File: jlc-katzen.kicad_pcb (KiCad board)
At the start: 2 copper layers, 50.8 x 50.8 mm, 46 parts, among them J1 USB_C_Receptacle_USB2.0_16P, J2 Conn_01x04, J3 Conn_01x04, J4 Conn_01x02, J5 Conn_ARM_SWD_TagConnect_TC2030, Q1 2N7002, Q2 2N7002, Q3 2N7002, U1 XC6206P332MR, U2 W25Q128JVSIQ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

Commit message: useless twiddles
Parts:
- moved J5 16.5 mm to (115.5, 42.1)
- moved J4 6.31 mm to (91.7, 62.1), turned to -90 degrees
- moved R2 4.12 mm to (87.0, 50.5)
- moved R1 4.03 mm to (87.0, 46.5)
- moved R10 3.04 mm to (94.5, 62.5)
- moved R8 2.55 mm to (94.5, 61.5)
- moved R6 2.50 mm to (91.0, 47.5)
- moved C17 2.23 mm to (87.5, 61.5)
- moved U2 2.06 mm to (90.5, 57.5)
- moved C16 1.80 mm to (100.0, 61.0)
- moved U4 1.80 mm to (103.5, 63.5)
- moved C8 1.58 mm to (106.0, 48.0)
- moved C9 1.58 mm to (106.0, 49.0)
- moved R3 1.58 mm to (106.0, 47.0)
- moved C13 1.12 mm to (97.0, 44.0)
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
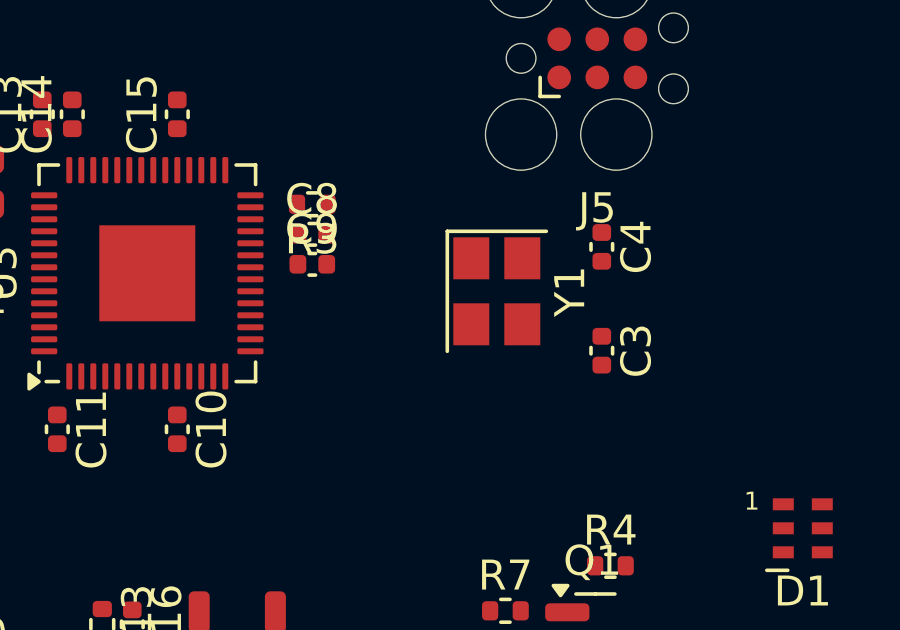
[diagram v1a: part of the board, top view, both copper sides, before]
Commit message: fix crystal
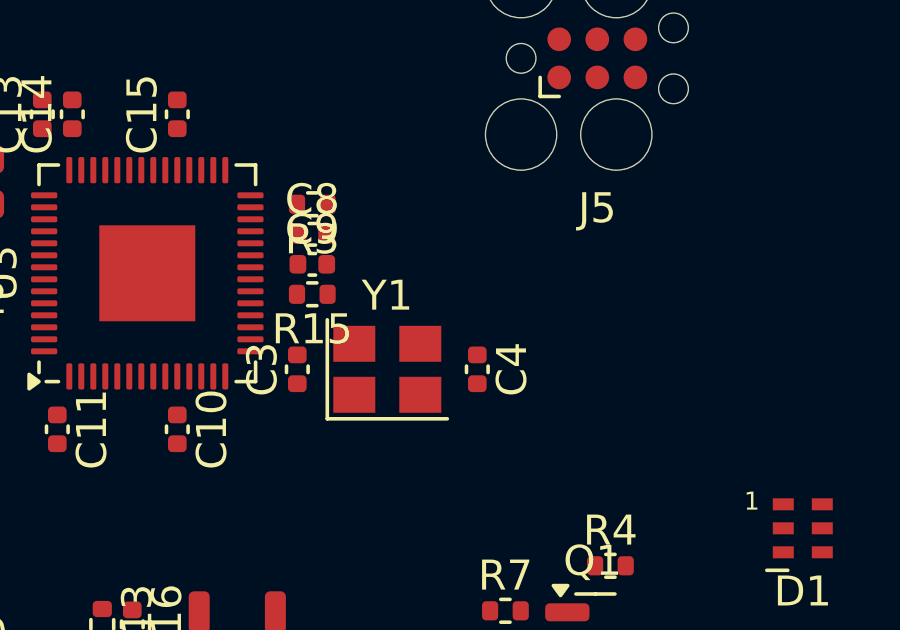
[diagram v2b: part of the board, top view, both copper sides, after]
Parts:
- added R15: 1k, Resistor_SMD:R_0402_1005Metric, F.Cu at (106.0, 50.0)
- moved C3 10.2 mm to (105.5, 52.5), turned to 90 degrees
- moved C4 5.82 mm to (111.5, 52.5)
- moved Y1 4.48 mm to (108.5, 52.5), turned to 0 degrees
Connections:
- net Net-(U3-XIN) renamed /XTAL_IN
- C4 pad 1: Net-(U3-XOUT) -> Net-(C4-Pad1)
- U3 pad 21: Net-(U3-XOUT) -> /XTAL_OUT
- Y1 pad 2: Net-(U3-XOUT) -> GND
- Y1 pad 3: (no net) -> Net-(C4-Pad1)
- Y1 pad 4: (no net) -> GND

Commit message: name some nets
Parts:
- turned R12 to 180 degrees
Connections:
- net Net-(C4-Pad1) renamed /XR
- net Net-(U2-CLK) renamed /FLASH_SCK
- net Net-(U2-DI(IO0)) renamed /FLASH_D0
- net Net-(U2-DO(IO1)) renamed /FLASH_D1
- net Net-(U2-IO2) renamed /FLASH_D2
- net Net-(U2-IO3) renamed /FLASH_D3
- net Net-(U2-~{CS}) renamed /FLASH_~{SS}
- net Net-(U3-USB_DM) renamed /USB_RP_D-
- net Net-(U3-USB_DP) renamed /USB_RP_D+

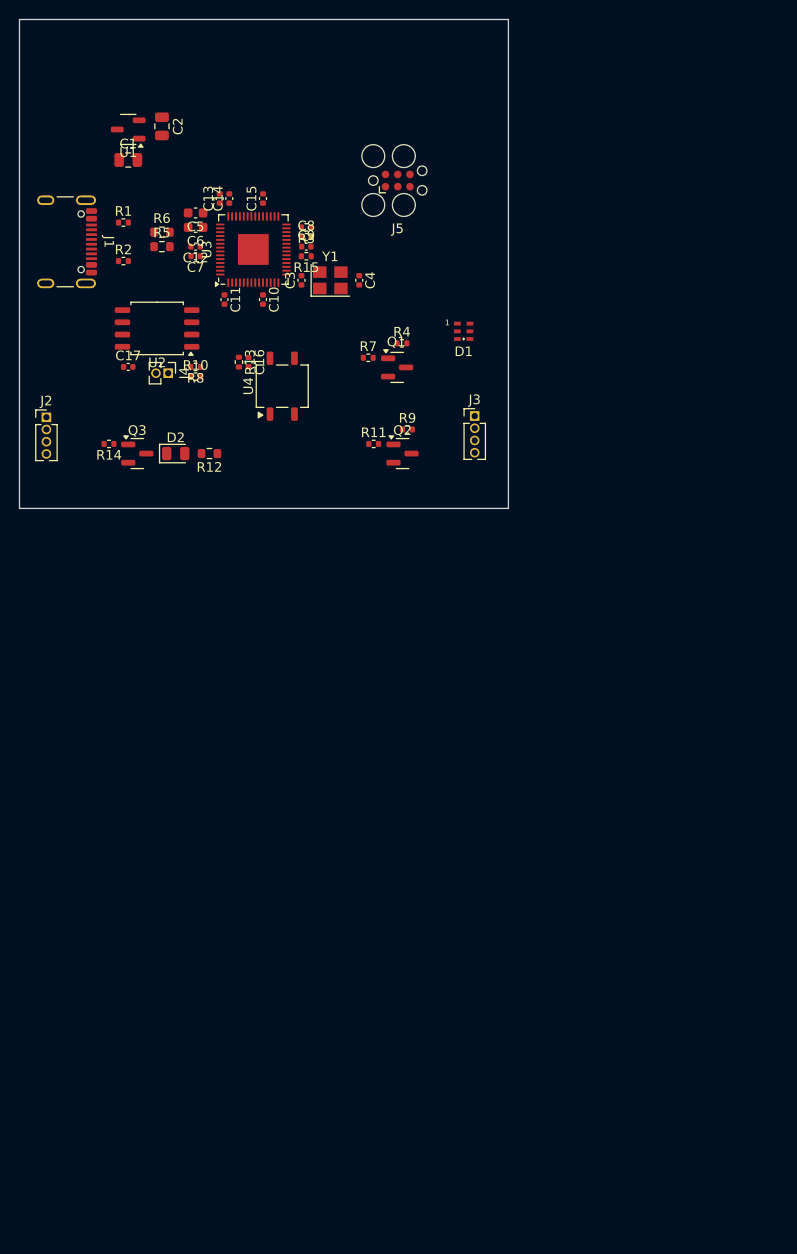
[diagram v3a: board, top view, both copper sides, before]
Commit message: hopefully fit this many leds
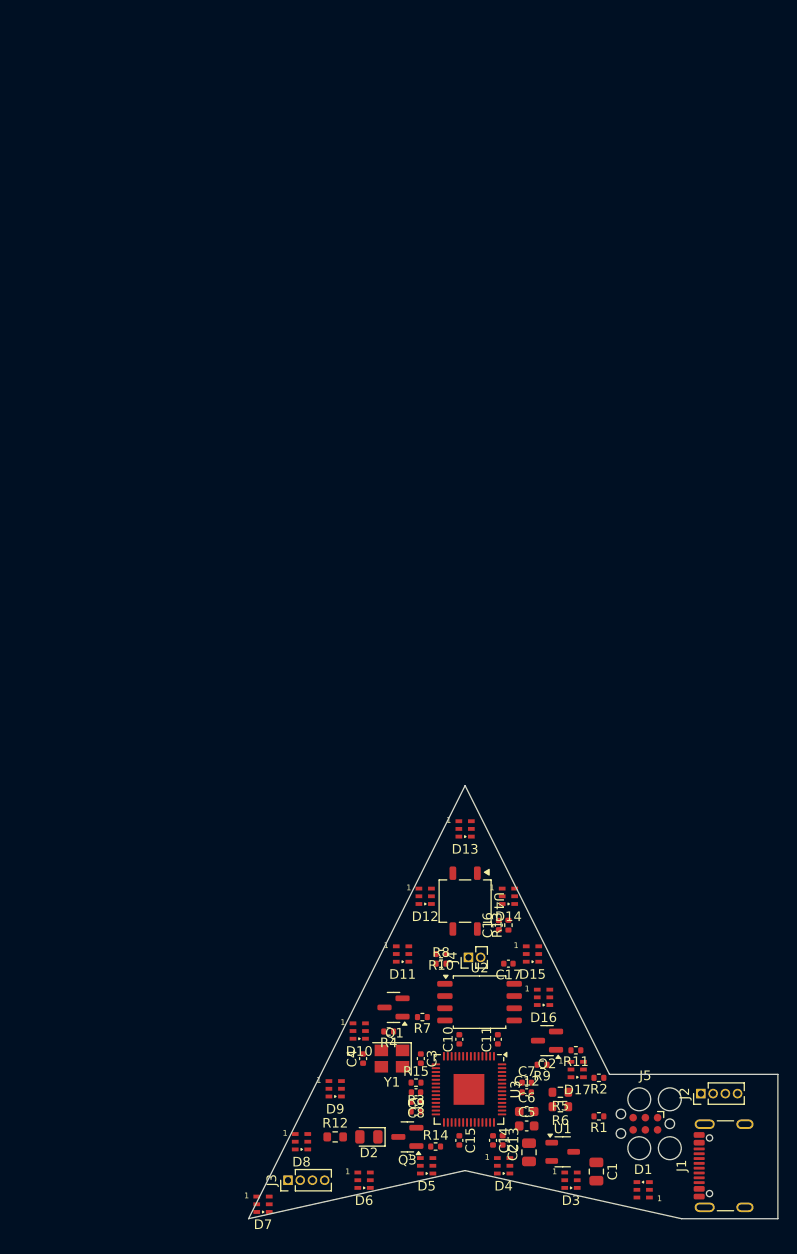
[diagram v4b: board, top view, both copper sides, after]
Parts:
- added D10: SK9822-2020, custom_parts:LED-SK9822-2020, F.Cu at (111.5, 130.5)
- added D11: SK9822-2020, custom_parts:LED-SK9822-2020, F.Cu at (116.0, 122.5)
- added D12: SK9822-2020, custom_parts:LED-SK9822-2020, F.Cu at (118.3, 116.5)
- added D13: SK9822-2020, custom_parts:LED-SK9822-2020, F.Cu at (122.5, 109.5)
- added D14: SK9822-2020, custom_parts:LED-SK9822-2020, F.Cu at (127.0, 116.5)
- added D15: SK9822-2020, custom_parts:LED-SK9822-2020, F.Cu at (129.5, 122.5)
- added D16: SK9822-2020, custom_parts:LED-SK9822-2020, F.Cu at (130.7, 127.0)
- added D17: SK9822-2020, custom_parts:LED-SK9822-2020, F.Cu at (134.2, 134.5)
- added D3: SK9822-2020, custom_parts:LED-SK9822-2020, F.Cu at (133.5, 146.0)
- added D4: SK9822-2020, custom_parts:LED-SK9822-2020, F.Cu at (126.5, 144.5)
- added D5: SK9822-2020, custom_parts:LED-SK9822-2020, F.Cu at (118.5, 144.5)
- added D6: SK9822-2020, custom_parts:LED-SK9822-2020, F.Cu at (112.0, 146.0)
- added D7: SK9822-2020, custom_parts:LED-SK9822-2020, F.Cu at (101.5, 148.5)
- added D8: SK9822-2020, custom_parts:LED-SK9822-2020, F.Cu at (105.5, 142.0)
- added D9: SK9822-2020, custom_parts:LED-SK9822-2020, F.Cu at (109.0, 136.5)
- moved J1 119.1 mm to (150.5, 144.5), turned to 90 degrees
- moved C1 115.8 mm to (136.1, 145.1), turned to -90 degrees
- moved U1 115.4 mm to (132.6, 143.1), turned to 0 degrees
- moved C2 113.2 mm to (129.1, 143.1), turned to 90 degrees
- moved R1 105.2 mm to (136.4, 139.4), turned to 180 degrees
- moved C13 102.2 mm to (126.4, 141.9), turned to -90 degrees
- moved C14 101.6 mm to (125.4, 141.9), turned to -90 degrees
- moved J5 101.3 mm to (141.2, 140.1), turned to 180 degrees
- moved C5 100.9 mm to (128.9, 140.4), turned to 0 degrees
- moved C15 100.0 mm to (121.9, 141.9), turned to -90 degrees
- moved R6 99.8 mm to (132.4, 138.4), turned to 180 degrees
- moved R2 98.2 mm to (136.4, 135.4), turned to 180 degrees
- moved C6 98.1 mm to (128.9, 138.9), turned to 0 degrees
- moved J2 97.8 mm to (147.0, 137.0), turned to 90 degrees
- moved R5 97.1 mm to (132.4, 136.9), turned to 180 degrees
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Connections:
- D1 pad 1: unconnected-(D1-SDO-Pad1) -> Net-(D1-SDO)
- D1 pad 6: unconnected-(D1-CKO-Pad6) -> Net-(D1-CKO)
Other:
- board size 50.8 x 50.8 mm -> 55 x 45 mm

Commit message: rough route
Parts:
- J5: moved to B.Cu
- moved R12 67.2 mm to (99.0, 75.0), turned to 90 degrees
- moved R14 66.5 mm to (108.0, 77.0), turned to -90 degrees
- moved D2 65.9 mm to (101.5, 76.5)
- moved Q3 65.9 mm to (105.5, 76.5)
- moved C1 58.2 mm to (140.0, 87.0), turned to 90 degrees
- moved R9 56.6 mm to (113.5, 80.0)
- moved C2 55.7 mm to (133.0, 87.5)
- moved U1 55.7 mm to (136.5, 87.5)
- moved R11 53.9 mm to (114.0, 82.5), turned to -90 degrees
- moved J1 53.7 mm to (146.3, 91.0)
- moved D1 53.6 mm to (128.0, 95.0), turned to 90 degrees
- moved Q2 53.0 mm to (111.5, 82.2)
- moved D3 52.0 mm to (121.0, 95.5), turned to 90 degrees
- moved J4 50.9 mm to (97.8, 78.5), turned to -90 degrees
- moved D14 49.7 mm to (103.0, 73.0), turned to -90 degrees
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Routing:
- net +5V: track 0.00 -> 176.3 mm, vias 0 -> 19
- net GND: track 0.00 -> 50.4 mm, vias 0 -> 44
- net /SWCLK: track 0.00 -> 47.6 mm, vias 0 -> 1
- net /~{RESET}: track 0.00 -> 42.9 mm, vias 0 -> 1
- net /SWDIO: track 0.00 -> 38.8 mm, vias 0 -> 1
- net /CC1: track 0.00 -> 37.8 mm, vias 0 -> 2
- net +3.3V: track 0.00 -> 35.9 mm, vias 0 -> 13
- net /CC2: track 0.00 -> 34.1 mm, vias 0 -> 2
- net /LED_DAT_5V: track 0.00 -> 32.7 mm, vias 0 -> 4
- net /USB_D+: track 0.00 -> 30.2 mm, vias 0 -> 2
- net /USB_D-: track 0.00 -> 29.1 mm
- net /FLASH_~{SS}: track 0.00 -> 19.5 mm, vias 0 -> 2
- net +1V1: track 0.00 -> 18.6 mm
- net /FLASH_D2: track 0.00 -> 17.5 mm, vias 0 -> 2
- net /FLASH_D1: track 0.00 -> 17.4 mm, vias 0 -> 2
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- added copper zone on In2.Cu, net +3.3V
- added copper zone on F.Cu, net GND
- added copper zone on In1.Cu, net GND
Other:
- board size 55 x 45 mm -> 59.4 x 52.2 mm
- copper layers 2 -> 4
- board text added: "1"
- board text added: "2"
- board text added: "3"
- board text added: "4"
- board text added: "Chuuni Rights!"

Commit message: all nets connected
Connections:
- U3 pad 13: unconnected-(U3-GPIO10-Pad13) -> /IR_TX
- U3 pad 14: unconnected-(U3-GPIO11-Pad14) -> /IR_RX
- U3 pad 15: unconnected-(U3-GPIO12-Pad15) -> /PAIR_IN_TX
- U3 pad 16: unconnected-(U3-GPIO13-Pad16) -> /PAIR_IN_RX
- U3 pad 2: /PAIR_IN_TX -> unconnected-(U3-GPIO0-Pad2)
- U3 pad 3: /PAIR_IN_RX -> unconnected-(U3-GPIO1-Pad3)
- U3 pad 31: unconnected-(U3-GPIO20-Pad31) -> /PAIR_OUT_TX
- U3 pad 32: unconnected-(U3-GPIO21-Pad32) -> /PAIR_OUT_RX
- U3 pad 6: /PAIR_OUT_TX -> unconnected-(U3-GPIO4-Pad6)
- U3 pad 7: /PAIR_OUT_RX -> unconnected-(U3-GPIO5-Pad7)
- U3 pad 8: /IR_RX -> unconnected-(U3-GPIO6-Pad8)
- U3 pad 9: /IR_TX -> unconnected-(U3-GPIO7-Pad9)
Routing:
- net /PAIR_IN_TX: track 0.00 -> 54.8 mm, vias 0 -> 4
- net /PAIR_IN_RX: track 0.00 -> 52.9 mm, vias 0 -> 4
- net /LED_CLK: track 0.00 -> 17.3 mm, vias 0 -> 2
- net /IR_TX: track 0.00 -> 15.2 mm
- net /PAIR_OUT_RX: track 0.00 -> 14.8 mm, vias 0 -> 2
- net /PAIR_OUT_TX: track 0.00 -> 13.6 mm, vias 0 -> 2
- net /IR_RX: track 0.00 -> 9.82 mm, vias 0 -> 2
- net /LED_DAT: track 0.00 -> 7.22 mm, vias 0 -> 2
- net GND: track 50.4 -> 52.4 mm, vias 44 -> 55
- net Net-(Q3-G): track 0.00 -> 1.59 mm
- net /FLASH_D2: track 17.5 -> 16.0 mm
- net /FLASH_D1: track 17.4 -> 16.3 mm
- net /CC2: track 34.1 -> 35.1 mm
- net /CC1: track 37.8 -> 38.8 mm
- net +3.3V: track 35.9 -> 36.9 mm, vias 13 -> 14
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
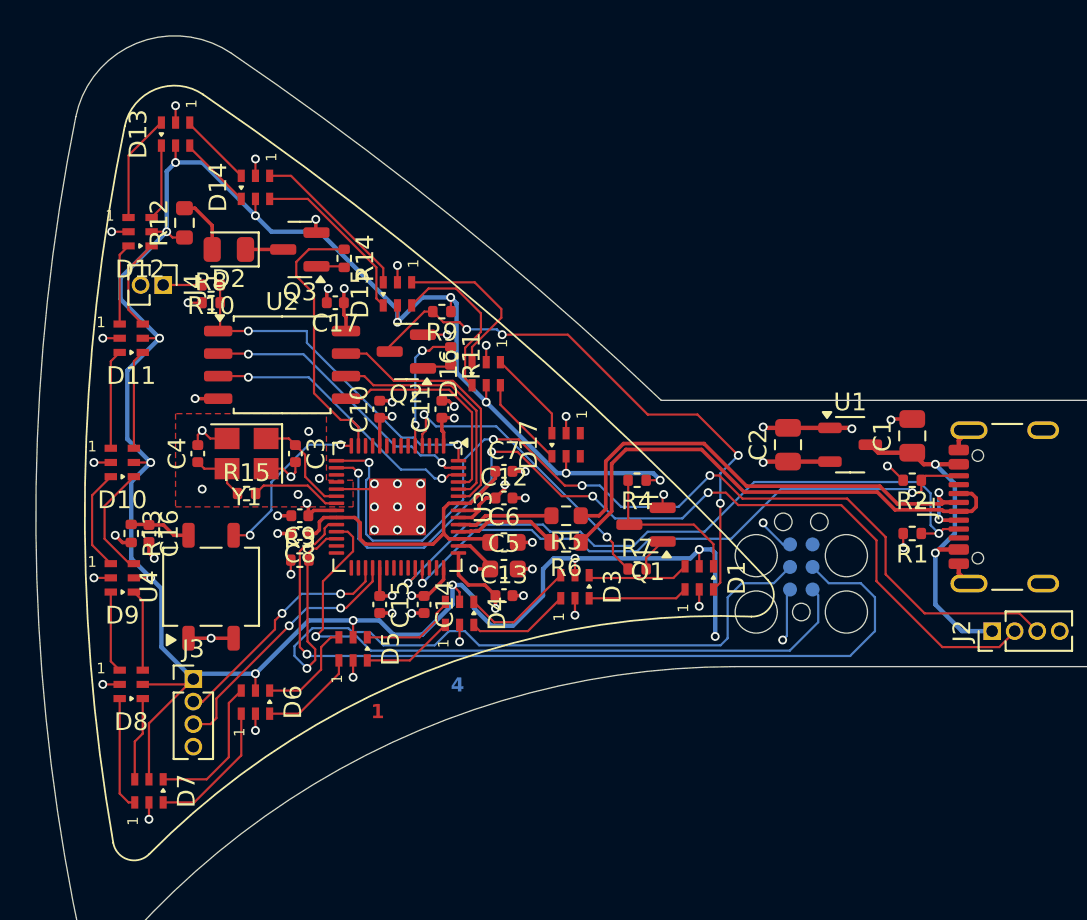
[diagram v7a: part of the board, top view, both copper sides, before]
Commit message: clean traces, hide refdes on silk
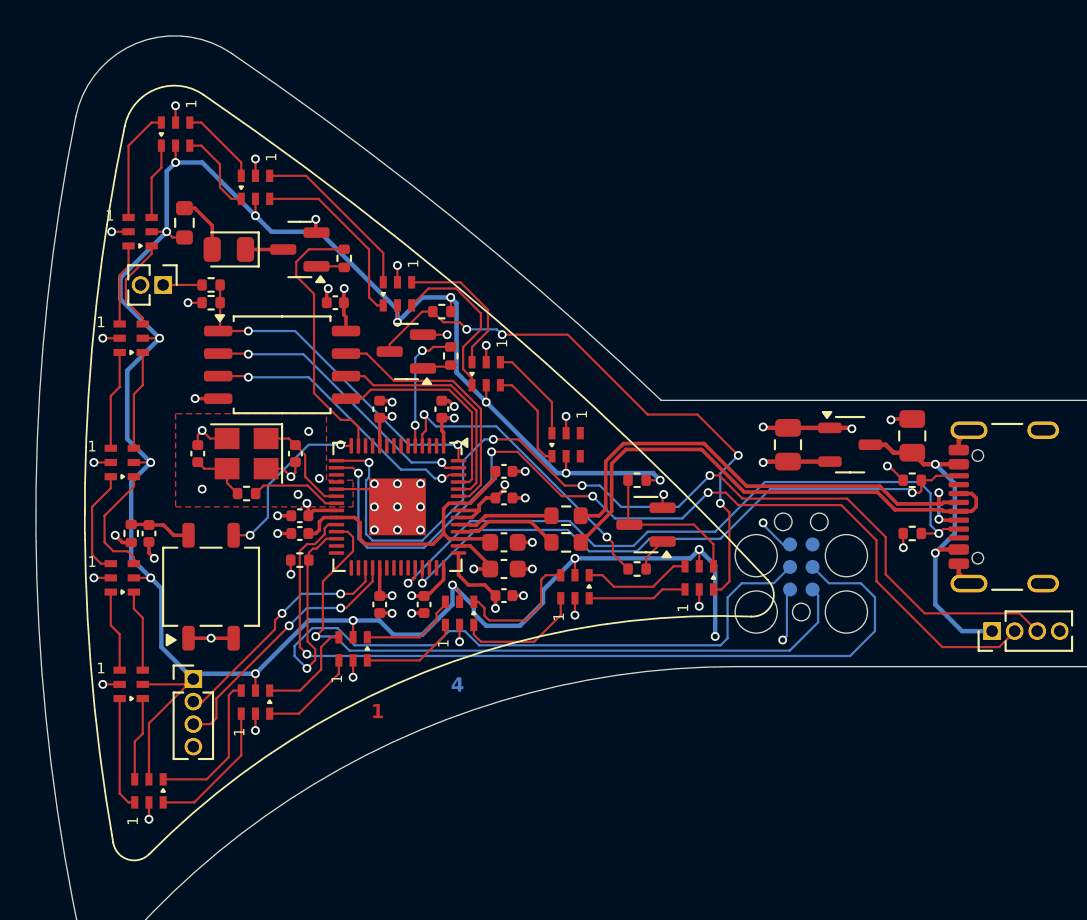
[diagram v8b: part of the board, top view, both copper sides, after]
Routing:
- net Net-(D3-SDO): track 5.81 -> 7.19 mm
- net Net-(D15-SDO): track 9.35 -> 8.26 mm
- net +5V: track 177.1 -> 176.1 mm
- net Net-(D3-CKO): track 6.47 -> 7.46 mm
- net /USB_D+: track 30.2 -> 29.3 mm
- net /LED_DAT_5V: track 32.2 -> 33.0 mm
- net Net-(D13-CKO): track 4.20 -> 4.90 mm
- net Net-(D16-CKO): track 5.20 -> 5.79 mm
- net Net-(D14-CKO): track 9.91 -> 10.5 mm
